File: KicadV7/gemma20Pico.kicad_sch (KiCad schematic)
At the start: 10 parts, among them J1-Prox1 I2C_CH0, J2-Prox0 I2C_CH1, J3-Motor1 DC-Motor, J4-BAT1 3.7V Battery, J5-Servo1 Servo, J6-Pot1 Pot, J7-Pot2 Pot, U1-RPI-Pico1 Pico

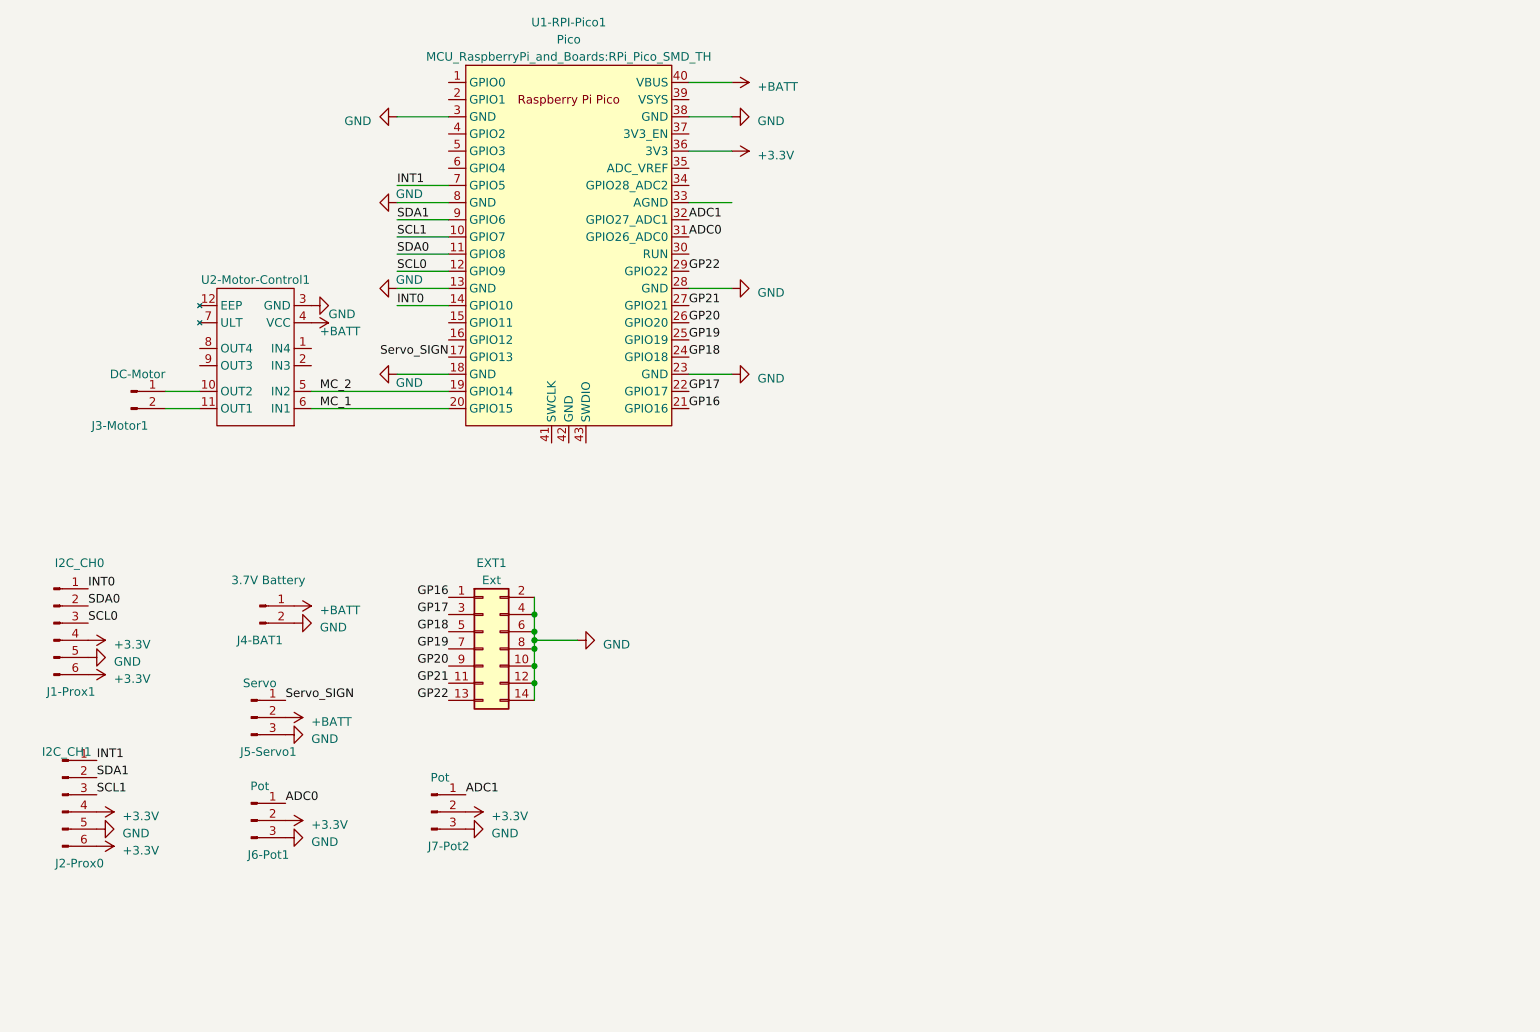
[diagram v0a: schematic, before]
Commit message: Added External components to the schematics
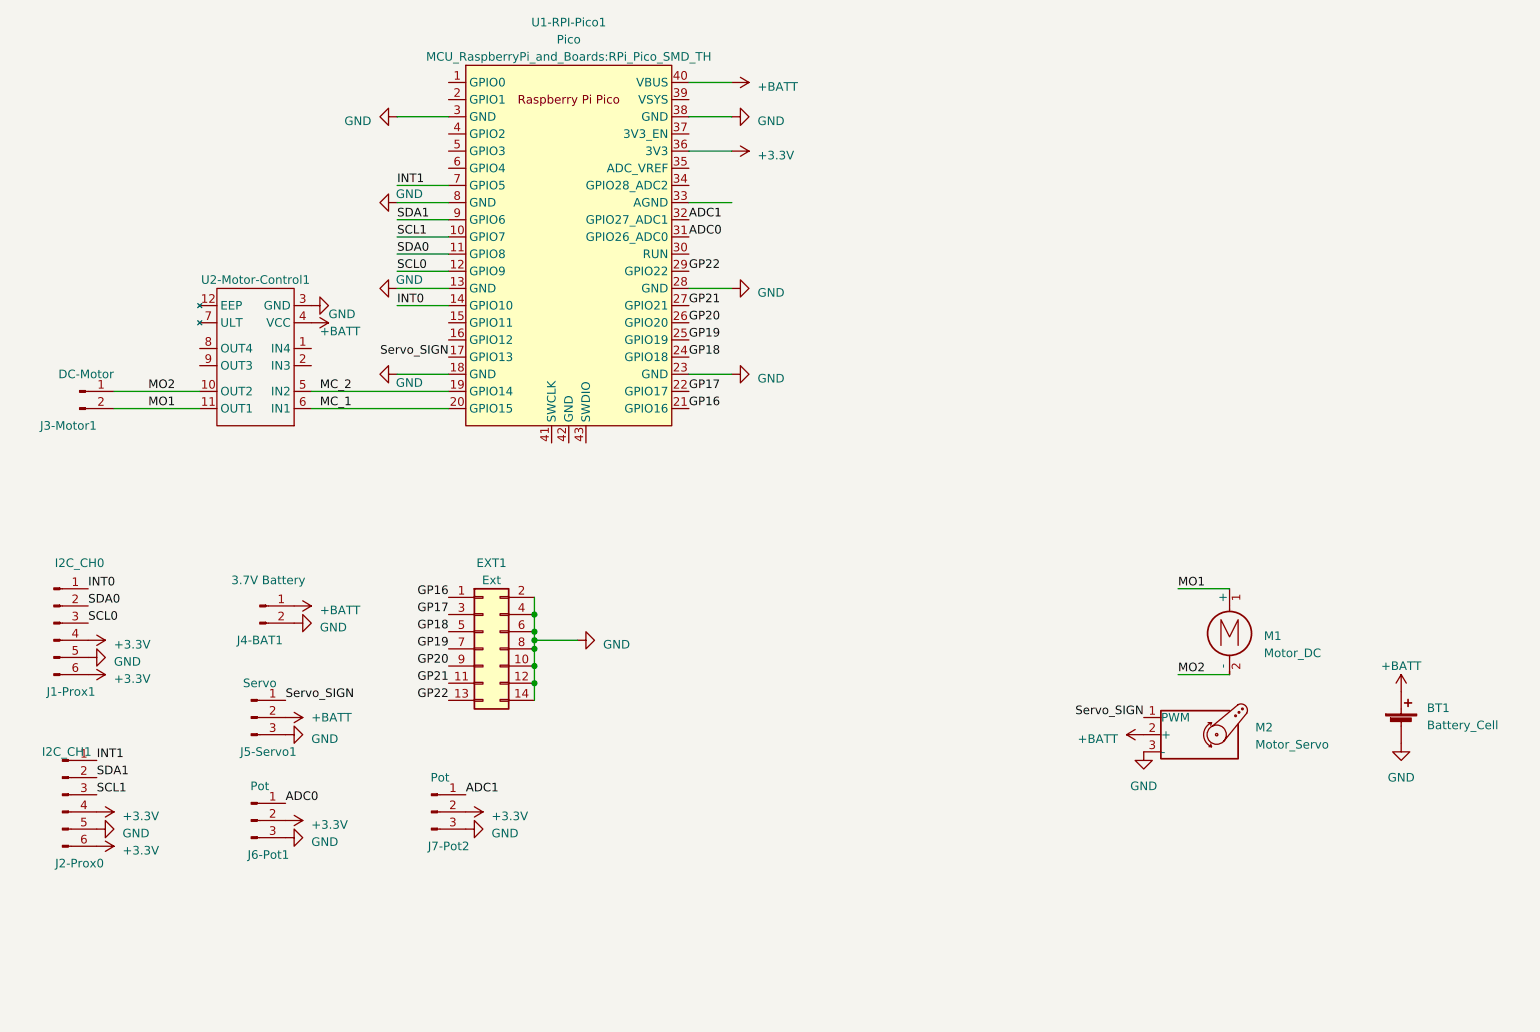
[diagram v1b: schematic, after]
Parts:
- added BT1: Battery_Cell, symbol Device:Battery_Cell
- added M1: Motor_DC, symbol Motor:Motor_DC
- added M2: Motor_Servo, symbol Motor:Motor_Servo
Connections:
- net +BATT: now also BT1.1 (+), M2.2 (+)
- net GND: now also BT1.2 (-), M2.3 (-)
- net Servo_SIGN: now also M2.1 (PWM)
- net MO2: now reaches J3-Motor1.1 (Pin_1), U2-Motor-Control1.10 (OUT2)
- net MO2: now also M1.2 (-)
- net MO1: now reaches J3-Motor1.2 (Pin_2), U2-Motor-Control1.11 (OUT1)
- net MO1: now also M1.1 (+)
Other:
- moved on the sheet: J3-Motor1
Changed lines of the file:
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@@
+    (stroke (width 0) (type default))
+  )
+  (wire (pts (xy 201.93 130.81) (xy 209.55 130.81))
     (stroke (width 0) (type default))
   )
@@
     (stroke (width 0) (type default))
   )
-  (wire (pts (xy 57.15 88.9) (xy 52.07 88.9))
+  (wire (pts (xy 57.15 88.9) (xy 44.45 88.9))
     (stroke (width 0) (type default))
   )
@@
     (stroke (width 0) (type default))
   )
+  (wire (pts (xy 201.93 118.11) (xy 209.55 118.11))
+    (stroke (width 0) (type default))
+  )
   (wire (pts (xy 129.54 48.26) (xy 135.89 48.26))
     (stroke (width 0) (type default))
@@
     (stroke (width 0) (type default))
   )
-  (wire (pts (xy 57.15 91.44) (xy 52.07 91.44))
+  (wire (pts (xy 57.15 91.44) (xy 44.45 91.44))
     (stroke (width 0) (type default))
   )
@@
     (effects (font (size 1.27 1.27)) (justify right bottom))
   )
+  (label "Servo_SIGN" (at 196.85 137.16 180) (fields_autoplaced)
+    (effects (font (size 1.27 1.27)) (justify right bottom))
+  )
   (label "GP16" (at 129.54 91.44 0) (fields_autoplaced)
+    (effects (font (size 1.27 1.27)) (justify left bottom))
+  )
+  (label "MO1" (at 49.53 91.44 0) (fields_autoplaced)
     (effects (font (size 1.27 1.27)) (justify left bottom))
   )
@@
     (effects (font (size 1.27 1.27)) (justify left bottom))
   )
+  (label "MO2" (at 201.93 130.81 0) (fields_autoplaced)
+    (effects (font (size 1.27 1.27)) (justify left bottom))
+  )
   (label "SCL1" (at 41.91 148.59 0) (fields_autoplaced)
     (effects (font (size 1.27 1.27)) (justify left bottom))
@@
   )
   (label "SCL0" (at 86.36 71.12 0) (fields_autoplaced)
+    (effects (font (size 1.27 1.27)) (justify left bottom))
+  )
+  (label "MO2" (at 49.53 88.9 0) (fields_autoplaced)
     (effects (font (size 1.27 1.27)) (justify left bottom))
   )
@@
     (effects (font (size 1.27 1.27)) (justify left bottom))
   )
+  (label "MO1" (at 201.93 118.11 0) (fields_autoplaced)
+    (effects (font (size 1.27 1.27)) (justify left bottom))
+  )
   (label "INT1" (at 86.36 58.42 0) (fields_autoplaced)
     (effects (font (size 1.27 1.27)) (justify left bottom))
@@
         (path "/b10b7441-68fa-49c0-9dad-fceb534010fc"
           (reference "#PWR03") (unit 1)
+        )
+      )
+    )
+  )
+  (symbol (lib_id "Motor:Motor_Servo") (at 204.47 139.7 0) (unit 1)
+    (in_bom yes) (on_board yes) (dnp no) (fields_autoplaced)
+    (property "Reference" "M2" (at 213.36 138.6316 0)
+      (effects (font (size 1.27 1.27)) (justify left))
+    )
+    (property "Value" "Motor_Servo" (at 213.36 141.1716 0)
+      (effects (font (size 1.27 1.27)) (justify left))
+    )
+    (property "Footprint" "" (at 204.47 144.526 0)
+      (effects (font (size 1.27 1.27)) hide)
+    )
+    (property "Datasheet" "http://forums.parallax.com/uploads/attachments/46831/74481.png" (at 204.47 144.526 0)
+      (effects (font (size 1.27 1.27)) hide)
+    )
+    (pin "1")
+    (pin "2")
+    (pin "3")
+    (instances
+      (project "gemma20Pico"
+        (path "/b10b7441-68fa-49c0-9dad-fceb534010fc"
+          (reference "M2") (unit 1)
+        )
+      )
+    )
+  )
+  (symbol (lib_id "Device:Battery_Cell") (at 234.95 138.43 0) (unit 1)
+    (in_bom yes) (on_board yes) (dnp no) (fields_autoplaced)
+    (property "Reference" "BT1" (at 238.76 135.763 0)
+      (effects (font (size 1.27 1.27)) (justify left))
+    )
+    (property "Value" "Battery_Cell" (at 238.76 138.303 0)
+      (effects (font (size 1.27 1.27)) (justify left))
+    )
+    (property "Footprint" "" (at 234.95 136.906 90)
+      (effects (font (size 1.27 1.27)) hide)
+    )
+    (property "Datasheet" "~" (at 234.95 136.906 90)
+      (effects (font (size 1.27 1.27)) hide)
+    )
+    (pin "1")
+    (pin "2")
+    (instances
+      (project "gemma20Pico"
+        (path "/b10b7441-68fa-49c0-9dad-fceb534010fc"
+          (reference "BT1") (unit 1)
         )
       )
@@
     )
   )
+  (symbol (lib_id "power:+BATT") (at 234.95 133.35 0) (unit 1)
+    (in_bom yes) (on_board yes) (dnp no) (fields_autoplaced)
+    (property "Reference" "#PWR030" (at 234.95 137.16 0)
+      (effects (font (size 1.27 1.27)) hide)
+    )
+    (property "Value" "+BATT" (at 234.95 129.54 0)
+      (effects (font (size 1.27 1.27)))
+    )
+    (property "Footprint" "" (at 234.95 133.35 0)
+      (effects (font (size 1.27 1.27)) hide)
+    )
+    (property "Datasheet" "" (at 234.95 133.35 0)
+      (effects (font (size 1.27 1.27)) hide)
+    )
+    (pin "1")
+    (instances
+      (project "gemma20Pico"
+        (path "/b10b7441-68fa-49c0-9dad-fceb534010fc"
+          (reference "#PWR030") (unit 1)
+        )
+      )
+    )
+  )
   (symbol (lib_id "power:GND") (at 71.12 123.19 90) (unit 1)
-    (in_bom yes) (on_board yes) (dnp no) (fields_autoplaced)
+    (in_bom yes) (on_board yes) (dnp no)
     (property "Reference" "#PWR017" (at 77.47 123.19 0)
       (effects (font (size 1.27 1.27)) hide)
@@
   )
   (symbol (lib_id "power:+BATT") (at 69.85 137.16 270) (unit 1)
-    (in_bom yes) (on_board yes) (dnp no) (fields_autoplaced)
+    (in_bom yes) (on_board yes) (dnp no)
     (property "Reference" "#PWR022" (at 66.04 137.16 0)
       (effects (font (size 1.27 1.27)) hide)
     )
-    (property "Value" "+BATT" (at 73.66 137.795 90)
+    (property "Value" "+BATT" (at 73.66 137.16 90)
       (effects (font (size 1.27 1.27)) (justify left))
     )
@@
         (path "/b10b7441-68fa-49c0-9dad-fceb534010fc"
           (reference "#PWR02") (unit 1)
+        )
+      )
+    )
+  )
+  (symbol (lib_id "power:+BATT") (at 196.85 139.7 90) (unit 1)
+    (in_bom yes) (on_board yes) (dnp no) (fields_autoplaced)
+    (property "Reference" "#PWR031" (at 200.66 139.7 0)
+      (effects (font (size 1.27 1.27)) hide)
+    )
+    (property "Value" "+BATT" (at 193.04 140.335 90)
+      (effects (font (size 1.27 1.27)) (justify left))
+    )
+    (property "Footprint" "" (at 196.85 139.7 0)
+      (effects (font (size 1.27 1.27)) hide)
+    )
+    (property "Datasheet" "" (at 196.85 139.7 0)
+      (effects (font (size 1.27 1.27)) hide)
+    )
+    (pin "1")
+    (instances
+      (project "gemma20Pico"
+        (path "/b10b7441-68fa-49c0-9dad-fceb534010fc"
+          (reference "#PWR031") (unit 1)
         )
       )
@@
     )
   )
+  (symbol (lib_id "power:GND") (at 196.85 142.24 0) (unit 1)
+    (in_bom yes) (on_board yes) (dnp no) (fields_autoplaced)
+    (property "Reference" "#PWR028" (at 196.85 148.59 0)
+      (effects (font (size 1.27 1.27)) hide)
+    )
+    (property "Value" "GND" (at 196.85 147.32 0)
+      (effects (font (size 1.27 1.27)))
+    )
+    (property "Footprint" "" (at 196.85 142.24 0)
+      (effects (font (size 1.27 1.27)) hide)
+    )
+    (property "Datasheet" "" (at 196.85 142.24 0)
+      (effects (font (size 1.27 1.27)) hide)
+    )
+    (pin "1")
+    (instances
+      (project "gemma20Pico"
+        (path "/b10b7441-68fa-49c0-9dad-fceb534010fc"
+          (reference "#PWR028") (unit 1)
+        )
+      )
+    )
+  )
   (symbol (lib_id "power:+BATT") (at 73.66 78.74 270) (unit 1)
     (in_bom yes) (on_board yes) (dnp no)
@@
     )
   )
-  (symbol (lib_id "Connector:Conn_01x02_Pin") (at 46.99 88.9 0) (unit 1)
-    (in_bom yes) (on_board yes) (dnp no)
-    (property "Reference" "J3-Motor1" (at 49.53 93.98 0)
-      (effects (font (size 1.27 1.27)) (justify right))
-    )
-    (property "Value" "DC-Motor" (at 52.07 86.36 0)
-      (effects (font (size 1.27 1.27)) (justify right))
-    )
-    (property "Footprint" "Connector_PinHeader_2.54mm:PinHeader_1x02_P2.54mm_Vertical" (at 46.99 88.9 0)
-      (effects (font (size 1.27 1.27)) hide)
-    )
-    (property "Datasheet" "~" (at 46.99 88.9 0)
+  (symbol (lib_id "Connector:Conn_01x02_Pin") (at 39.37 88.9 0) (unit 1)
+    (in_bom yes) (on_board yes) (dnp no)
+    (property "Reference" "J3-Motor1" (at 41.91 93.98 0)
+      (effects (font (size 1.27 1.27)) (justify right))
+    )
+    (property "Value" "DC-Motor" (at 44.45 86.36 0)
+      (effects (font (size 1.27 1.27)) (justify right))
+    )
+    (property "Footprint" "Connector_PinHeader_2.54mm:PinHeader_1x02_P2.54mm_Vertical" (at 39.37 88.9 0)
+      (effects (font (size 1.27 1.27)) hide)
+    )
+    (property "Datasheet" "~" (at 39.37 88.9 0)
       (effects (font (size 1.27 1.27)) hide)
     )
@@
         (path "/b10b7441-68fa-49c0-9dad-fceb534010fc"
           (reference "#PWR021") (unit 1)
+        )
+      )
+    )
+  )
+  (symbol (lib_id "Motor:Motor_DC") (at 209.55 123.19 0) (unit 1)
+    (in_bom yes) (on_board yes) (dnp no) (fields_autoplaced)
+    (property "Reference" "M1" (at 214.63 125.095 0)
+      (effects (font (size 1.27 1.27)) (justify left))
+    )
+    (property "Value" "Motor_DC" (at 214.63 127.635 0)
+      (effects (font (size 1.27 1.27)) (justify left))
+    )
+    (property "Footprint" "" (at 209.55 125.476 0)
+      (effects (font (size 1.27 1.27)) hide)
+    )
+    (property "Datasheet" "~" (at 209.55 125.476 0)
+      (effects (font (size 1.27 1.27)) hide)
+    )
+    (pin "1")
+    (pin "2")
+    (instances
+      (project "gemma20Pico"
+        (path "/b10b7441-68fa-49c0-9dad-fceb534010fc"
+          (reference "M1") (unit 1)
         )
       )
@@
         )
       )
+    )
+  )
+  (symbol (lib_id "power:GND") (at 234.95 140.97 0) (unit 1)
+    (in_bom yes) (on_board yes) (dnp no) (fields_autoplaced)
+    (property "Reference" "#PWR027" (at 234.95 147.32 0)
+      (effects (font (size 1.27 1.27)) hide)
+    )
+    (property "Value" "GND" (at 234.95 146.05 0)
+      (effects (font (size 1.27 1.27)))
+    )
+    (property "Footprint" "" (at 234.95 140.97 0)
+      (effects (font (size 1.27 1.27)) hide)
+    )
+    (property "Datasheet" "" (at 234.95 140.97 0)
+      (effects (font (size 1.27 1.27)) hide)
+    )
+    (pin "1")
+    (instances
+      (project "gemma20Pico"
+        (path "/b10b7441-68fa-49c0-9dad-fceb534010fc"
+          (reference "#PWR027") (unit 1)
+        )
+      )
